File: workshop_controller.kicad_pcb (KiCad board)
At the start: 4 copper layers, 184.9 x 88 mm, 61 parts, among them J1 Conn_02x10_Odd_Even, J2 Conn_02x10_Odd_Even, J3 AudioJack3, J4 Micro_SD_Card, J5 Conn_02x25_Odd_Even, J6 Conn_01x05_Female, J7 LOGO_TOUCH, M1 Microphone4, SW1 SW_Push, SW2 SW_Push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

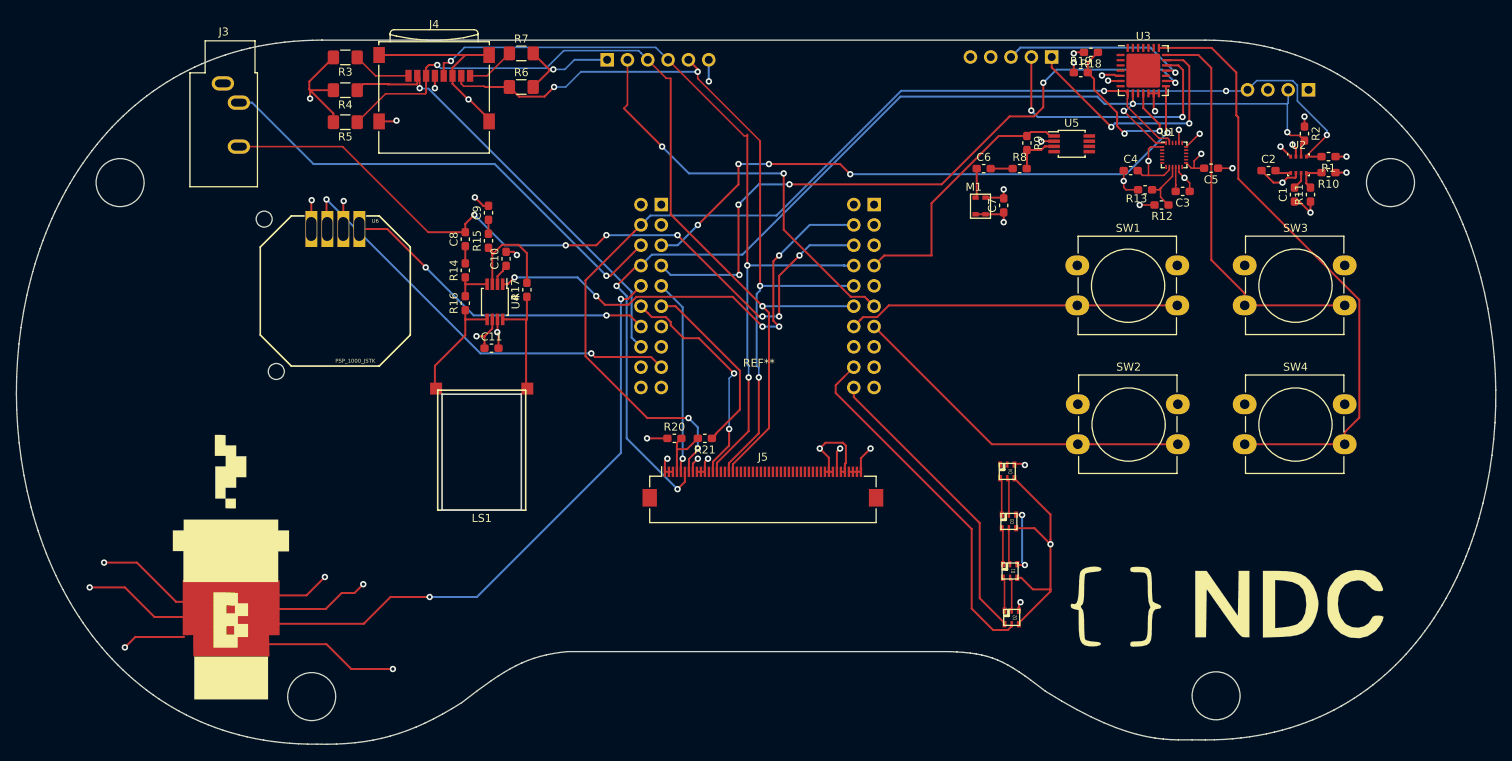
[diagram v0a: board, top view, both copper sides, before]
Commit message: Label resistors and capacitors
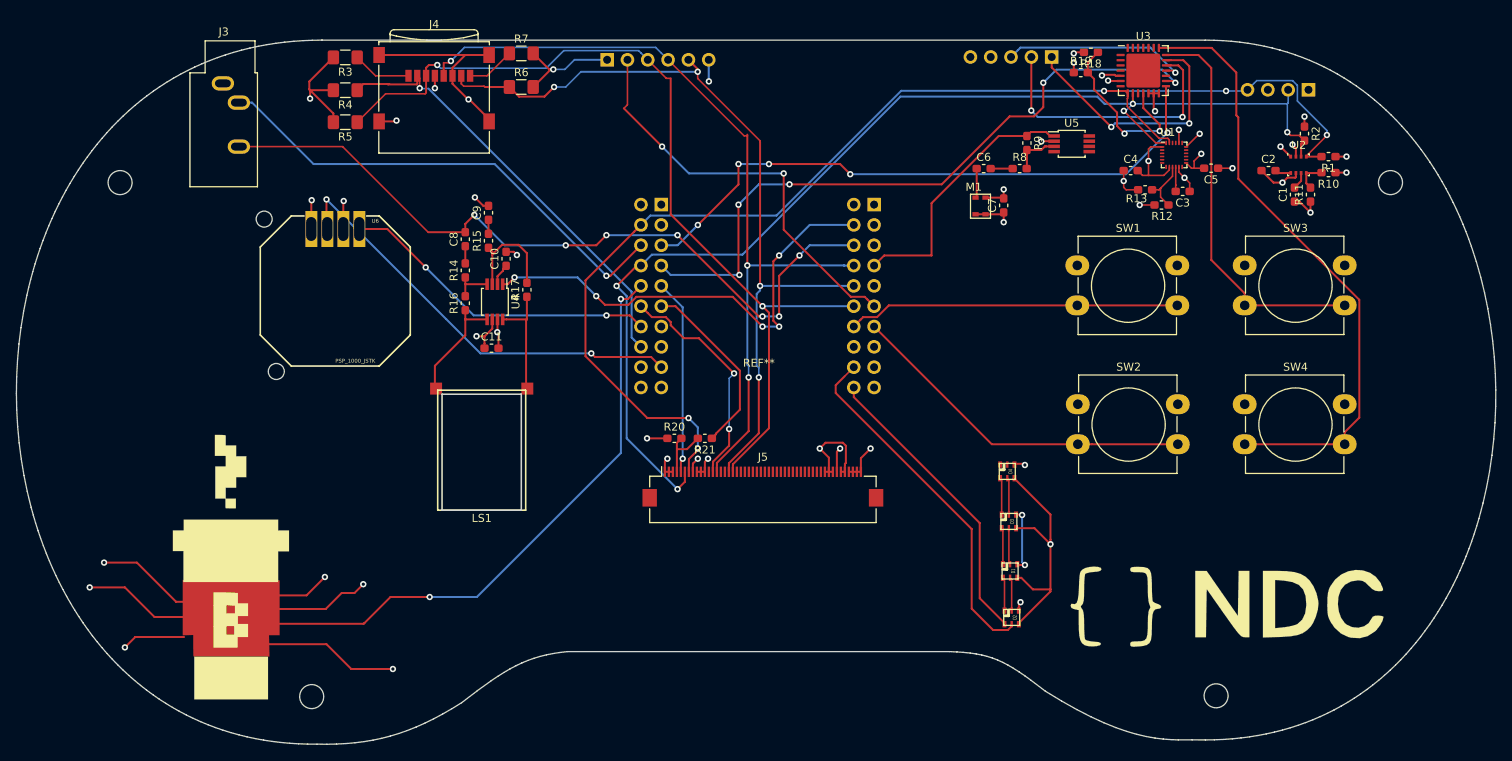
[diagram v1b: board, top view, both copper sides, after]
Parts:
- C10: value C_Small -> 0.1µF
- R1, R2: value 4.7kohm -> 4.7kΩ
- R10, R11, R12, R13, R18, R19, R20, R21: value R_Small -> 0Ω
- R3, R4, R5, R6, R7: value 50kOhm -> 50kΩ
- R8, R9: value ?ohm -> ?Ω
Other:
- outline, holes or cut-outs redrawn
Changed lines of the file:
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@@
       (effects (font (size 1 1) (thickness 0.15)))
     )
-    (fp_text value 50kOhm (at 0 1.82 180) (layer F.Fab)
+    (fp_text value 50kΩ (at 0 1.82 180) (layer F.Fab)
       (effects (font (size 1 1) (thickness 0.15)))
     )
@@
       (effects (font (size 1 1) (thickness 0.15)))
     )
-    (fp_text value 50kOhm (at 0 1.82) (layer F.Fab)
+    (fp_text value 50kΩ (at 0 1.82) (layer F.Fab)
       (effects (font (size 1 1) (thickness 0.15)))
     )
@@
       (effects (font (size 1 1) (thickness 0.15)))
     )
-    (fp_text value 50kOhm (at 0 1.82) (layer F.Fab)
+    (fp_text value 50kΩ (at 0 1.82) (layer F.Fab)
       (effects (font (size 1 1) (thickness 0.15)))
     )
@@
       (effects (font (size 1 1) (thickness 0.15)))
     )
-    (fp_text value 50kOhm (at 0 1.82 180) (layer F.Fab)
+    (fp_text value 50kΩ (at 0 1.82 180) (layer F.Fab)
       (effects (font (size 1 1) (thickness 0.15)))
     )
@@
       (effects (font (size 1 1) (thickness 0.15)))
     )
-    (fp_text value 50kOhm (at 0 1.82 180) (layer F.Fab)
+    (fp_text value 50kΩ (at 0 1.82 180) (layer F.Fab)
       (effects (font (size 1 1) (thickness 0.15)))
     )
@@
       (effects (font (size 1 1) (thickness 0.15)))
     )
-    (fp_text value 4.7kohm (at 0 1.43 180) (layer F.Fab)
+    (fp_text value 4.7kΩ (at 0 1.43 180) (layer F.Fab)
       (effects (font (size 1 1) (thickness 0.15)))
     )
@@
       (effects (font (size 1 1) (thickness 0.15)))
     )
-    (fp_text value 4.7kohm (at 0 1.43 270) (layer F.Fab)
+    (fp_text value 4.7kΩ (at 0 1.43 270) (layer F.Fab)
       (effects (font (size 1 1) (thickness 0.15)))
     )
@@
       (effects (font (size 1 1) (thickness 0.15)))
     )
-    (fp_text value ?ohm (at 0 1.43) (layer F.Fab)
+    (fp_text value ?Ω (at 0 1.43) (layer F.Fab)
       (effects (font (size 1 1) (thickness 0.15)))
     )
@@
       (effects (font (size 1 1) (thickness 0.15)))
     )
-    (fp_text value ?ohm (at 0 1.43 270) (layer F.Fab)
+    (fp_text value ?Ω (at 0 1.43 270) (layer F.Fab)
       (effects (font (size 1 1) (thickness 0.15)))
     )
@@
       (effects (font (size 1 1) (thickness 0.15)))
     )
-    (fp_text value R_Small (at 0 1.43 180) (layer F.Fab)
+    (fp_text value 0Ω (at 0 1.43 180) (layer F.Fab)
       (effects (font (size 1 1) (thickness 0.15)))
     )
@@
       (effects (font (size 1 1) (thickness 0.15)))
     )
-    (fp_text value R_Small (at 0 1.43 90) (layer F.Fab)
+    (fp_text value 0Ω (at 0 1.43 90) (layer F.Fab)
       (effects (font (size 1 1) (thickness 0.15)))
     )
@@
       (effects (font (size 1 1) (thickness 0.15)))
     )
-    (fp_text value R_Small (at 0 1.43) (layer F.Fab)
+    (fp_text value 0Ω (at 0 1.43) (layer F.Fab)
       (effects (font (size 1 1) (thickness 0.15)))
     )
@@
       (effects (font (size 1 1) (thickness 0.15)))
     )
-    (fp_text value R_Small (at 0 1.43 180) (layer F.Fab)
+    (fp_text value 0Ω (at 0 1.43 180) (layer F.Fab)
       (effects (font (size 1 1) (thickness 0.15)))
     )
@@
       (effects (font (size 1 1) (thickness 0.15)))
     )
-    (fp_text value C_Small (at 0 1.43 90) (layer F.Fab)
+    (fp_text value 0.1µF (at 0 1.43 90) (layer F.Fab)
       (effects (font (size 1 1) (thickness 0.15)))
     )
@@
       (effects (font (size 1 1) (thickness 0.15)))
     )
-    (fp_text value R_Small (at 0 1.43 180) (layer F.Fab)
+    (fp_text value 0Ω (at 0 1.43 180) (layer F.Fab)
       (effects (font (size 1 1) (thickness 0.15)))
     )
@@
       (effects (font (size 1 1) (thickness 0.15)))
     )
-    (fp_text value R_Small (at 0 1.43) (layer F.Fab)
+    (fp_text value 0Ω (at 0 1.43) (layer F.Fab)
       (effects (font (size 1 1) (thickness 0.15)))
     )
@@
       (effects (font (size 1 1) (thickness 0.15)))
     )
-    (fp_text value R_Small (at 0 1.43) (layer F.Fab)
+    (fp_text value 0Ω (at 0 1.43) (layer F.Fab)
       (effects (font (size 1 1) (thickness 0.15)))
     )
@@
       (effects (font (size 1 1) (thickness 0.15)))
     )
-    (fp_text value R_Small (at 0 1.43 180) (layer F.Fab)
+    (fp_text value 0Ω (at 0 1.43 180) (layer F.Fab)
       (effects (font (size 1 1) (thickness 0.15)))
     )
@@
     (arrow2b (pts (xy 152.081588 128.048429) (xy 151.492367 126.923387)))
   )
-  (gr_circle (center 212.1 135.05) (end 215.1 135.05) (layer Edge.Cuts) (width 0.15))
-  (gr_circle (center 233.9 70.9) (end 236.9 70.9) (layer Edge.Cuts) (width 0.15))
-  (gr_circle (center 99.05 135.15) (end 102.05 135.15) (layer Edge.Cuts) (width 0.15))
-  (gr_circle (center 75.1 70.9) (end 78.1 70.9) (layer Edge.Cuts) (width 0.15))
+  (gr_circle (center 212.1 135.05) (end 213.6 135.05) (layer Edge.Cuts) (width 0.15))
+  (gr_circle (center 233.9 70.9) (end 235.4 70.9) (layer Edge.Cuts) (width 0.15))
+  (gr_circle (center 99.05 135.15) (end 100.55 135.15) (layer Edge.Cuts) (width 0.15))
+  (gr_circle (center 75.1 70.9) (end 76.6 70.9) (layer Edge.Cuts) (width 0.15))
   (gr_line (start 87.978715 139.351603) (end 87.019888 139.021057) (layer Edge.Cuts) (width 0.1))
   (gr_line (start 87.019888 139.021057) (end 86.079005 138.664052) (layer Edge.Cuts) (width 0.1))

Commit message: Wip
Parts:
- added SW5: SW_Push, Hackheim_logo:contact_snes_button, F.Cu at (201.1, 83.8)
- added SW6: SW_Push, Hackheim_logo:contact_snes_button, F.Cu at (201.2, 101.1)
- added SW7: SW_Push, Hackheim_logo:contact_snes_button, F.Cu at (222.0, 83.8)
- added SW8: SW_Push, Hackheim_logo:contact_snes_button, F.Cu at (222.1, 101.1)
- added svg2mod: G***, svg2mod, F.Cu at (0.00, 0.00)
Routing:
- net /SW4_PIN: track 77.0 -> 80.4 mm
- net /PIN_5: track 41.5 -> 44.4 mm
- net /PIN_TMS: track 44.1 -> 46.8 mm
- net /SW3_PIN: track 50.2 -> 52.9 mm

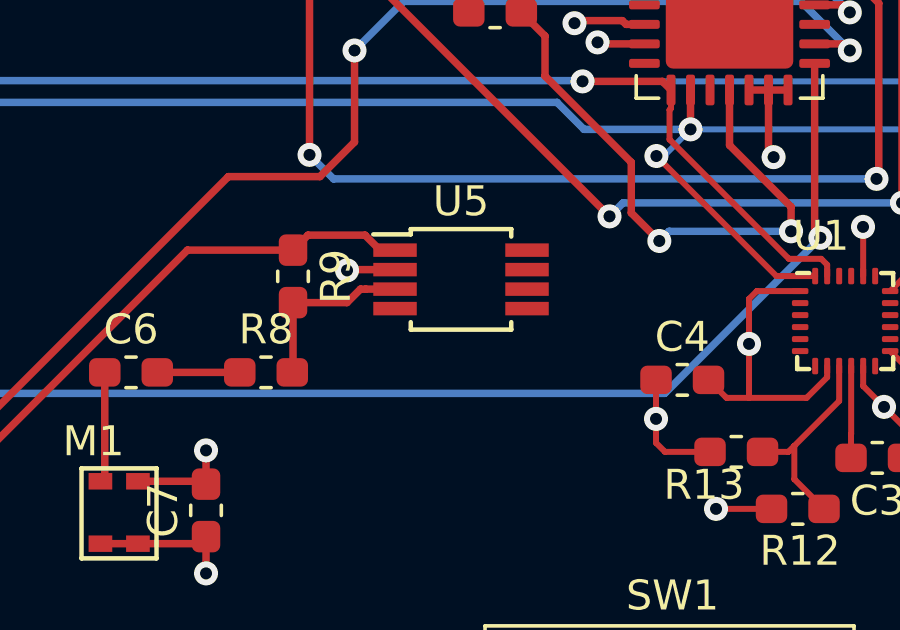
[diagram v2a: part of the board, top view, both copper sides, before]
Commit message: Fix microphone amp circuit
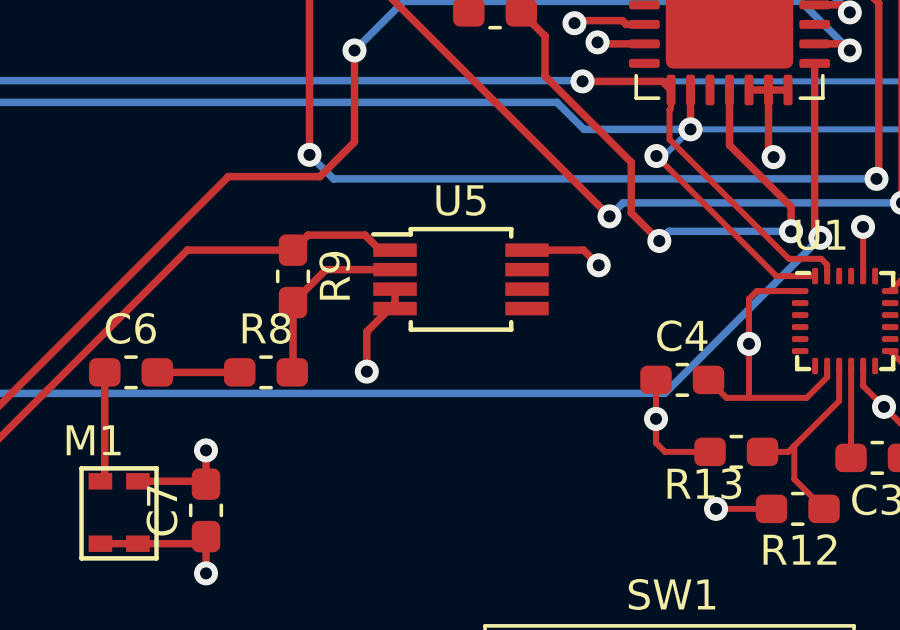
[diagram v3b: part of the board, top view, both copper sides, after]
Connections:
- U5 pad 2: +3V3 -> Net-(R8-Pad2)
- U5 pad 3: Net-(R8-Pad2) -> GND
- U5 pad 4: Net-(U5-Pad4) -> GND
- U5 pad 8: Net-(U5-Pad8) -> +3V3
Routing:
- net GND: track 120.4 -> 123.6 mm, vias 23 -> 24
- net +3V3: track 101.2 -> 102.2 mm
